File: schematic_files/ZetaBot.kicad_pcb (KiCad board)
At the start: 2 copper layers, 241.5 x 110.5 mm, 17 parts, among them J1 USB C PD Modulle, J2 Conn_01x05, J3 MOTOR_L, J4 MOTOR_R, SW1 SW_SPDT, U1 RPI5, U1 RPLIDAR C1, U2 Buck Converter

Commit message: 2nd revision. DRC passed.
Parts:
- added ?: , , F.Cu at (38.2, 121.2)
- added ?: , , F.Cu at (134.2, 121.6)
- added ?: , , F.Cu at (133.8, 61.2)
- added ?: , , F.Cu at (38.2, 61.2)
- J2: footprint Connector_PinHeader_2.54mm:PinHeader_1x05_P2.54mm_Vertical -> ZetaBotFootprints:PinHeader_1x05_P2.54mm_Vertical
- U1: footprint epsilon:RPI5 -> ZetaBotFootprints:RPI5
- moved F1 1.70 mm to (189.6, 128.7)
- moved C1 1.17 mm to (184.3, 51.4)
- moved C3 0.30 mm to (60.0, 114.1)
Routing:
- net PWM_L: track 321.2 -> 314.0 mm
- net +5V: track 403.9 -> 402.4 mm
- net Net-(F1-Pad2): track 27.9 -> 27.0 mm
- net Net-(SW1-B): track 13.2 -> 12.3 mm
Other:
- outline, holes or cut-outs redrawn
- board text added: "BP"
- board text added: "Zeta-Bot"
- board text removed: "Epsilon-Bot"
- board text removed: "SA"

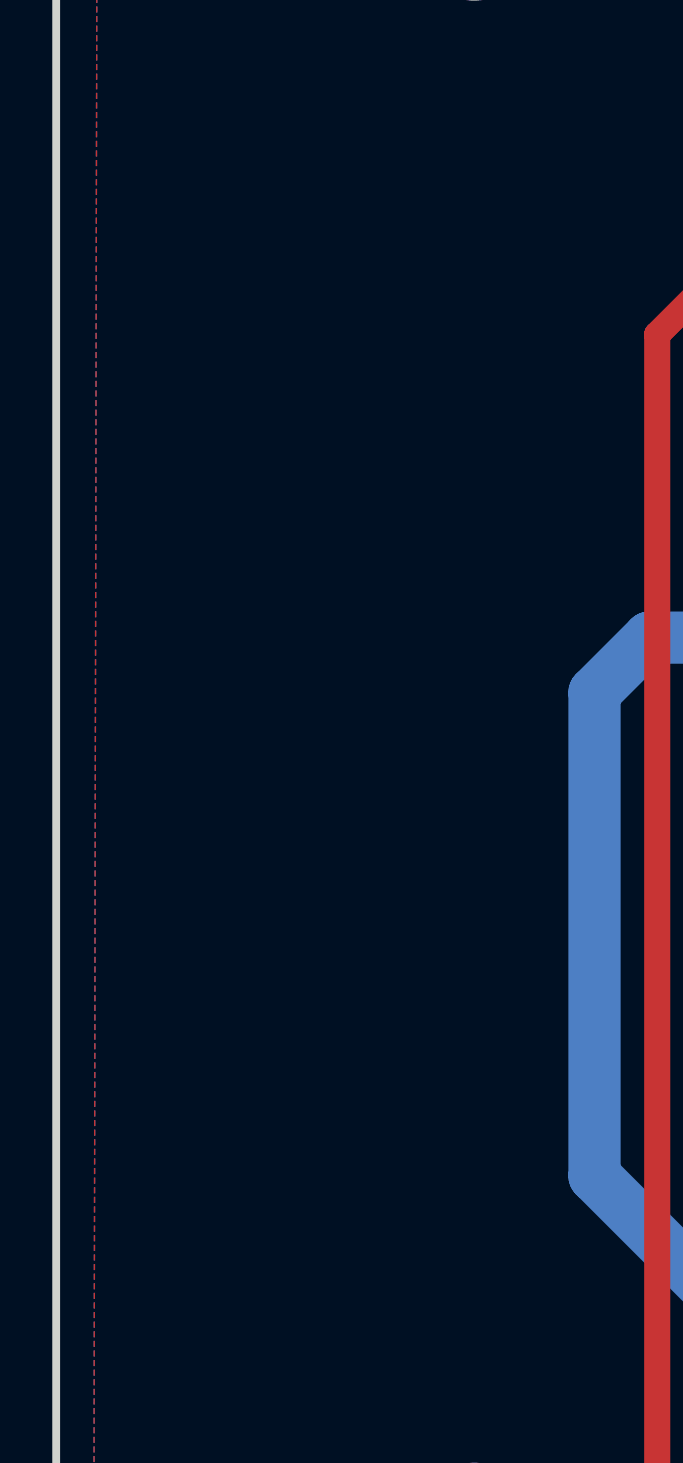
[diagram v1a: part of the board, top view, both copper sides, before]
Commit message: Added two holes for the caster ball.
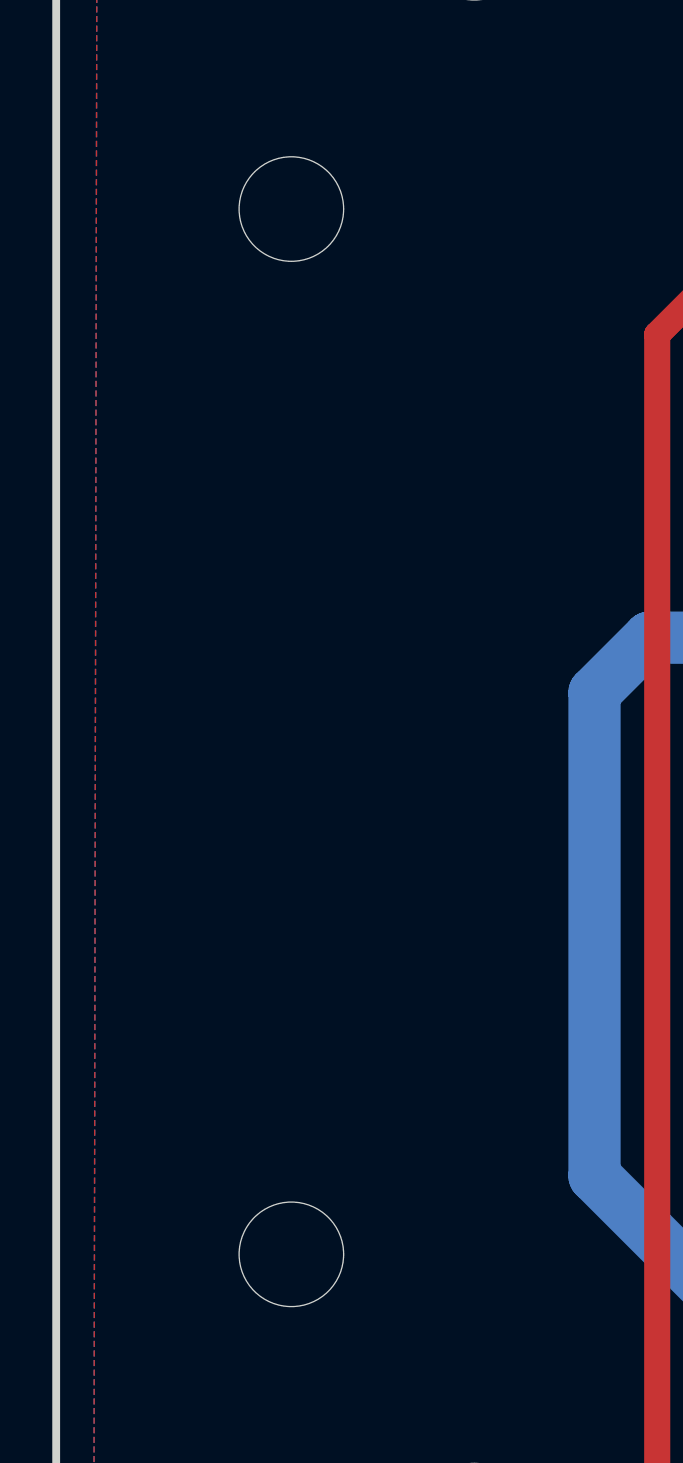
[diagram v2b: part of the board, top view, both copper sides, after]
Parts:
- added ?: , , F.Cu at (36.6, 71.0)
- added ?: , , F.Cu at (36.0, 111.0)
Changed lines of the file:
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@@
+	(footprint ""
+		(layer "F.Cu")
+		(at 36.6 71)
+		(property "Reference" ""
+			(at 0 0 0)
+			(layer "F.SilkS")
+			(effects
+				(font
+					(size 1.27 1.27)
+				)
+			)
+		)
+		(property "Value" ""
+			(at 0 0 0)
+			(layer "F.Fab")
+			(effects
+				(font
+					(size 1.27 1.27)
+				)
+			)
+		)
+		(property "Datasheet" ""
+			(at 0 0 0)
+			(layer "F.Fab")
+			(hide yes)
+			(effects
+				(font
+					(size 1.27 1.27)
+				)
+			)
+		)
+		(property "Description" ""
+			(at 0 0 0)
+			(layer "F.Fab")
+			(hide yes)
+			(effects
+				(font
+					(size 1.27 1.27)
+				)
+			)
+		)
+		(duplicate_pad_numbers_are_jumpers no)
+		(pad "" np_thru_hole circle
+			(at -0.6 0 90)
+			(size 4 4)
+			(drill 4)
+			(layers "*.Cu" "*.Mask")
+			(thermal_bridge_angle 90)
+		)
+		(embedded_fonts no)
+	)
 	(footprint ""
 		(layer "F.Cu")
@@
 		)
 		(embedded_fonts no)
+	)
+	(footprint ""
+		(layer "F.Cu")
+		(at 36 111)
+		(property "Reference" ""
+			(at 0 0 0)
+			(layer "F.SilkS")
+			(effects
+				(font
+					(size 1.27 1.27)
+				)
+			)
+		)
+		(property "Value" ""
+			(at 0 0 0)
+			(layer "F.Fab")
+			(effects
+				(font
+					(size 1.27 1.27)
+				)
+			)
+		)
+		(property "Datasheet" ""
+			(at 0 0 0)
+			(layer "F.Fab")
+			(hide yes)
+			(effects
+				(font
+					(size 1.27 1.27)
+				)
+			)
+		)
+		(property "Description" ""
+			(at 0 0 0)
+			(layer "F.Fab")
+			(hide yes)
+			(effects
+				(font
+					(size 1.27 1.27)
+				)
+			)
+		)
+		(duplicate_pad_numbers_are_jumpers no)
+		(pad "" np_thru_hole circle
+			(at 0 0 90)
+			(size 4 4)
+			(drill 4)
+			(layers "*.Cu" "*.Mask")
+			(thermal_bridge_angle 90)
+		)
+		(embedded_fonts no)
